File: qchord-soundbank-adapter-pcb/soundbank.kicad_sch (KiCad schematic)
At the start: 2 parts, among them U1 8MB ROM, U2 8MB Flash

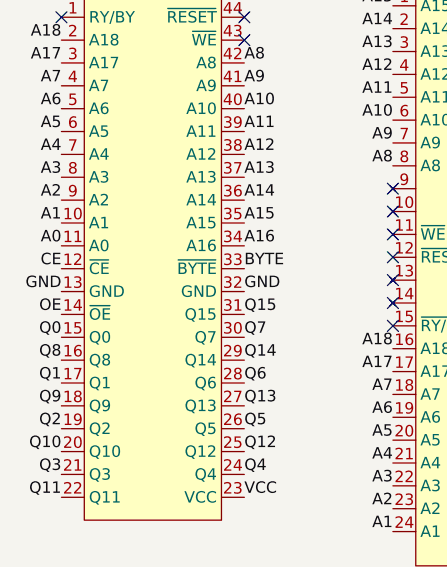
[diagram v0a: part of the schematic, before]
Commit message: Makes room for neighboring IC
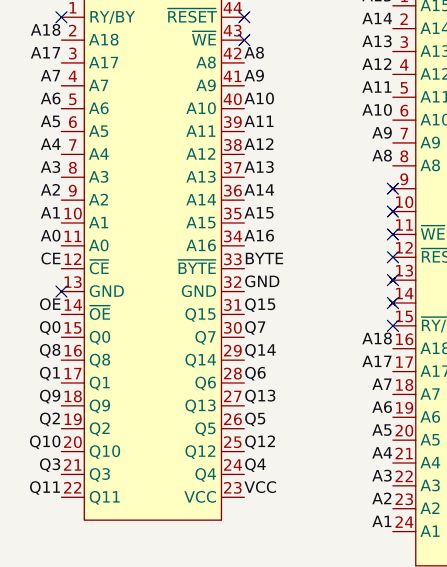
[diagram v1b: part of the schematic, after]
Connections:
- net GND: no longer U1.13 (GND)
- no-connect marks 10 -> 11
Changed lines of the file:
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@@
   (no_connect (at 139.7 113.03))
   (no_connect (at 139.7 110.49))
+  (no_connect (at 102.87 111.76))
   (no_connect (at 139.7 105.41))
   (no_connect (at 123.19 81.28))
@@
     (effects (font (size 1.27 1.27)) (justify right bottom))
   )
-  (label "GND" (at 102.87 111.76 180) (fields_autoplaced)
-    (effects (font (size 1.27 1.27)) (justify right bottom))
-  )

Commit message: Don't leave stuff floating
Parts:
- U1: value 8MB ROM -> 8Mbit ROM
- U2: value 8MB Flash -> 8Mbit Flash
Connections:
- net BYTE: now also U2.11 (~{WE}), U2.12 (~{RESET})
- no-connect marks 11 -> 9
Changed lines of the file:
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@@
   (paper "A4")
   (no_connect (at 139.7 115.57))
-  (no_connect (at 139.7 107.95))
   (no_connect (at 139.7 113.03))
   (no_connect (at 139.7 110.49))
   (no_connect (at 102.87 111.76))
-  (no_connect (at 139.7 105.41))
   (no_connect (at 123.19 81.28))
   (no_connect (at 102.87 81.28))
@@
     (effects (font (size 1.27 1.27)) (justify left bottom))
   )
+  (label "BYTE" (at 139.7 107.95 180) (fields_autoplaced)
+    (effects (font (size 1.27 1.27)) (justify right bottom))
+  )
   (label "A6" (at 102.87 91.44 180) (fields_autoplaced)
     (effects (font (size 1.27 1.27)) (justify right bottom))
@@
   (label "VCC" (at 186.69 107.95 0) (fields_autoplaced)
     (effects (font (size 1.27 1.27)) (justify left bottom))
+  )
+  (label "BYTE" (at 139.7 105.41 180) (fields_autoplaced)
+    (effects (font (size 1.27 1.27)) (justify right bottom))
   )
   (label "Q1" (at 102.87 121.92 180) (fields_autoplaced)
@@
       (effects (font (size 1.27 1.27)))
     )
-    (property "Value" "8MB Flash" (at 163.195 74.93 0)
+    (property "Value" "8Mbit Flash" (at 163.195 74.93 0)
       (effects (font (size 1.27 1.27)))
     )
@@
       (effects (font (size 1.27 1.27)) hide)
     )
-    (property "Datasheet" "" (at 139.7 71.12 0)
+    (property "Datasheet" "https://pdf1.alldatasheet.com/datasheet-pdf/view/934280/MCNIX/MX29F800CTTI-70G.html" (at 139.7 71.12 0)
       (effects (font (size 1.27 1.27)) hide)
+    )
+    (property "Notes" "" (at 139.7 71.12 0)
+      (effects (font (size 1.27 1.27)))
     )
     (pin "1")
@@
       (effects (font (size 1.27 1.27)))
     )
-    (property "Value" "8MB ROM" (at 113.03 77.47 0)
+    (property "Value" "8Mbit ROM" (at 113.03 77.47 0)
       (effects (font (size 1.27 1.27)))
     )
@@
       (effects (font (size 1.27 1.27)) hide)
     )
+    (property "Notes" "" (at 105.41 77.47 0)
+      (effects (font (size 1.27 1.27)))
+    )
     (pin "1")

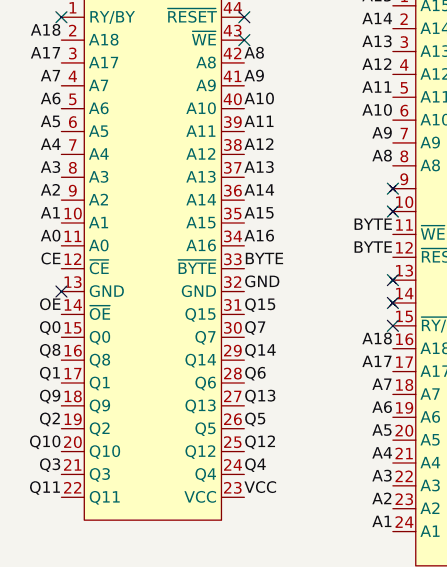
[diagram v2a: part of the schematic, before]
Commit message: add extra GND
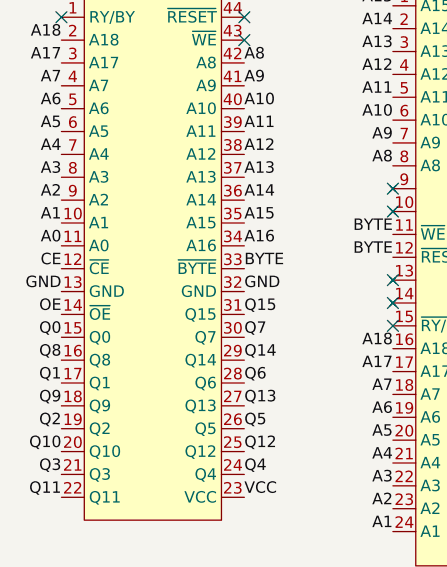
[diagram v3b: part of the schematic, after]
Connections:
- net GND: now also U1.13 (GND)
- no-connect marks 9 -> 8
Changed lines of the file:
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@@
   (no_connect (at 139.7 113.03))
   (no_connect (at 139.7 110.49))
-  (no_connect (at 102.87 111.76))
   (no_connect (at 123.19 81.28))
   (no_connect (at 102.87 81.28))
@@
     (effects (font (size 1.27 1.27)) (justify right bottom))
   )
+  (label "GND" (at 102.87 111.76 180) (fields_autoplaced)
+    (effects (font (size 1.27 1.27)) (justify right bottom))
+  )

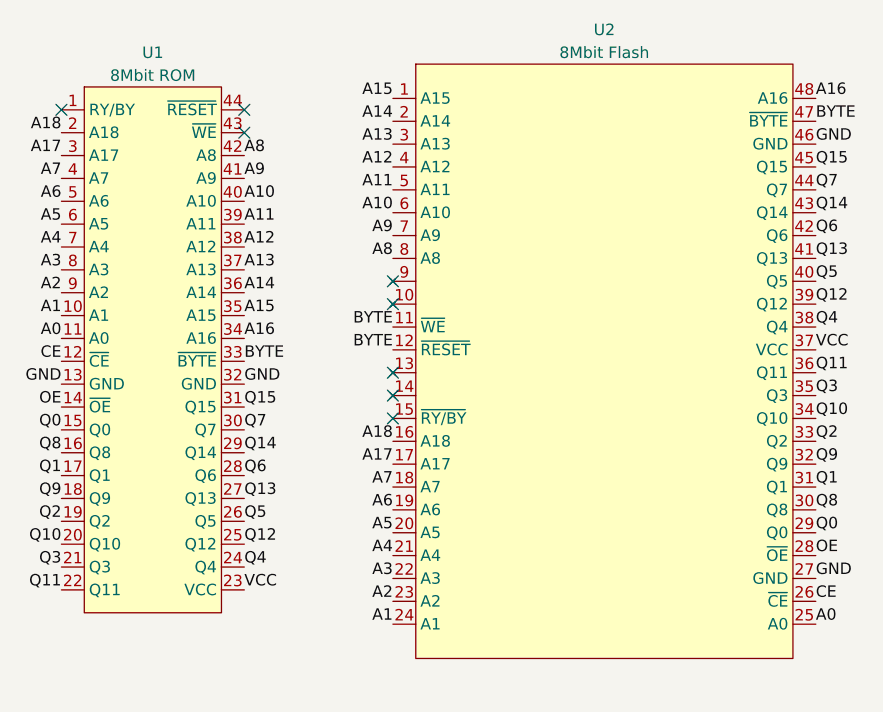
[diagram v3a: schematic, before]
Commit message: Adds some docs, pre-reversed Q616 dump
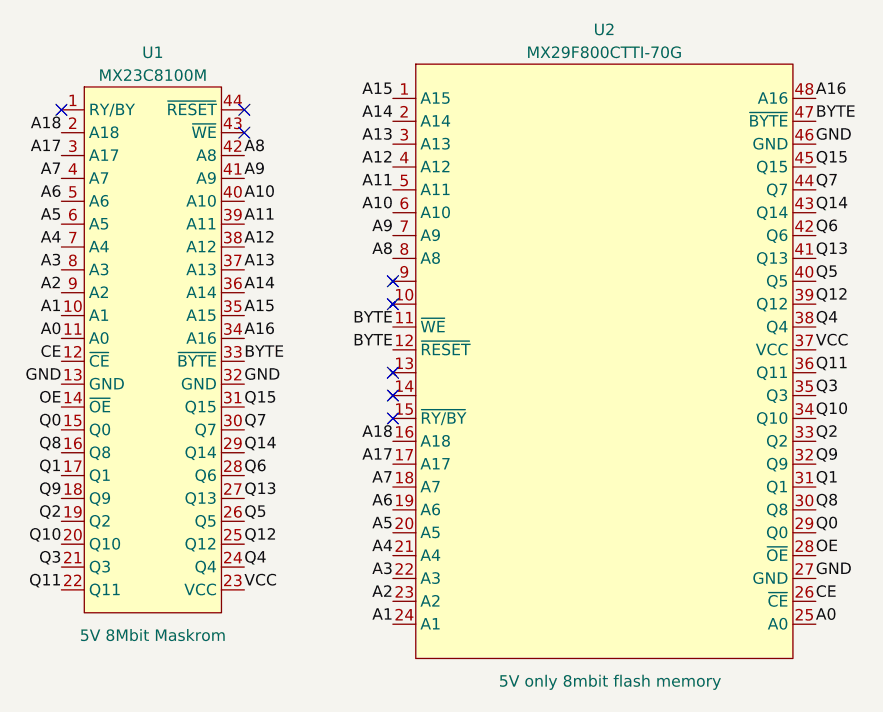
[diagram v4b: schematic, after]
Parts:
- U1: value 8Mbit ROM -> MX23C8100M; Notes (none) -> 5V 8Mbit Maskrom
- U2: value 8Mbit Flash -> MX29F800CTTI-70G; Notes (none) -> 5V only 8mbit flash memory
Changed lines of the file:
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@@
   )
   (symbol (lib_id "QChord_Soundbank:MX29F800CTTI") (at 139.7 71.12 0) (unit 1)
-    (in_bom yes) (on_board yes) (dnp no) (fields_autoplaced)
+    (in_bom yes) (on_board yes) (dnp no)
     (property "Reference" "U2" (at 163.195 72.39 0)
       (effects (font (size 1.27 1.27)))
     )
-    (property "Value" "8Mbit Flash" (at 163.195 74.93 0)
+    (property "Value" "MX29F800CTTI-70G" (at 163.195 74.93 0)
       (effects (font (size 1.27 1.27)))
     )
@@
       (effects (font (size 1.27 1.27)) hide)
     )
-    (property "Notes" "" (at 139.7 71.12 0)
+    (property "Notes" "5V only 8mbit flash memory" (at 163.83 144.78 0)
       (effects (font (size 1.27 1.27)))
     )
@@
       (effects (font (size 1.27 1.27)))
     )
-    (property "Value" "8Mbit ROM" (at 113.03 77.47 0)
+    (property "Value" "MX23C8100M" (at 113.03 77.47 0)
       (effects (font (size 1.27 1.27)))
     )
@@
       (effects (font (size 1.27 1.27)) hide)
     )
-    (property "Datasheet" "" (at 105.41 77.47 0)
+    (property "Datasheet" "https://pdf1.alldatasheet.com/datasheet-pdf/view/74427/MCNIX/MX23C8100.html" (at 105.41 77.47 0)
       (effects (font (size 1.27 1.27)) hide)
     )
-    (property "Notes" "" (at 105.41 77.47 0)
+    (property "Notes" "5V 8Mbit Maskrom" (at 113.03 139.7 0)
       (effects (font (size 1.27 1.27)))
     )
